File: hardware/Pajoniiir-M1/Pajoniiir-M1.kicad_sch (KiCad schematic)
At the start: 0 parts

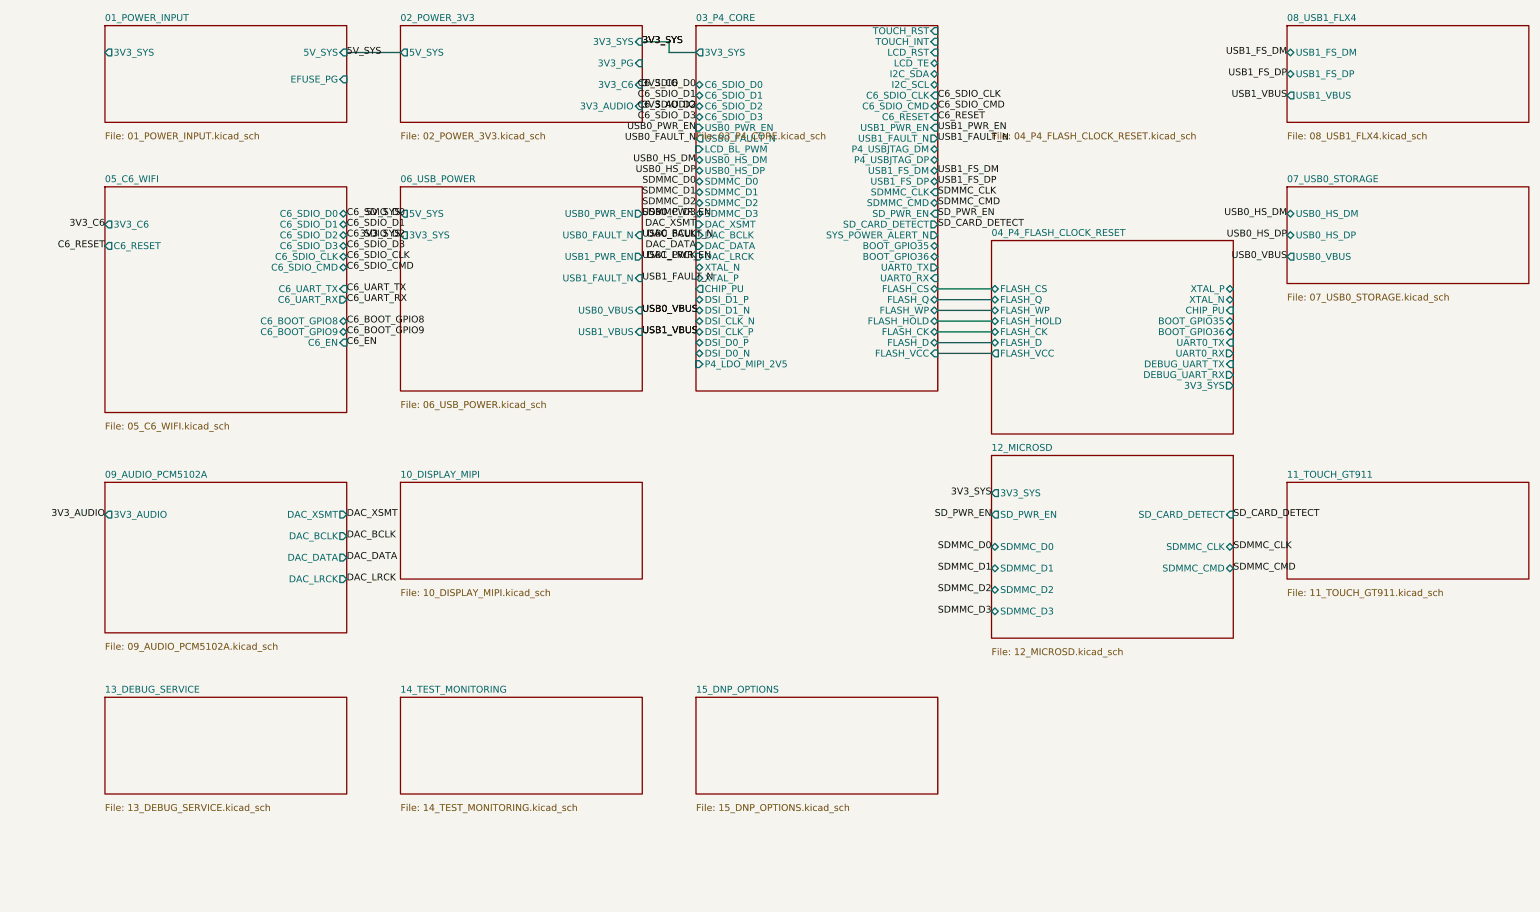
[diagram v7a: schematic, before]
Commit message: hardware: wire debug service hierarchy
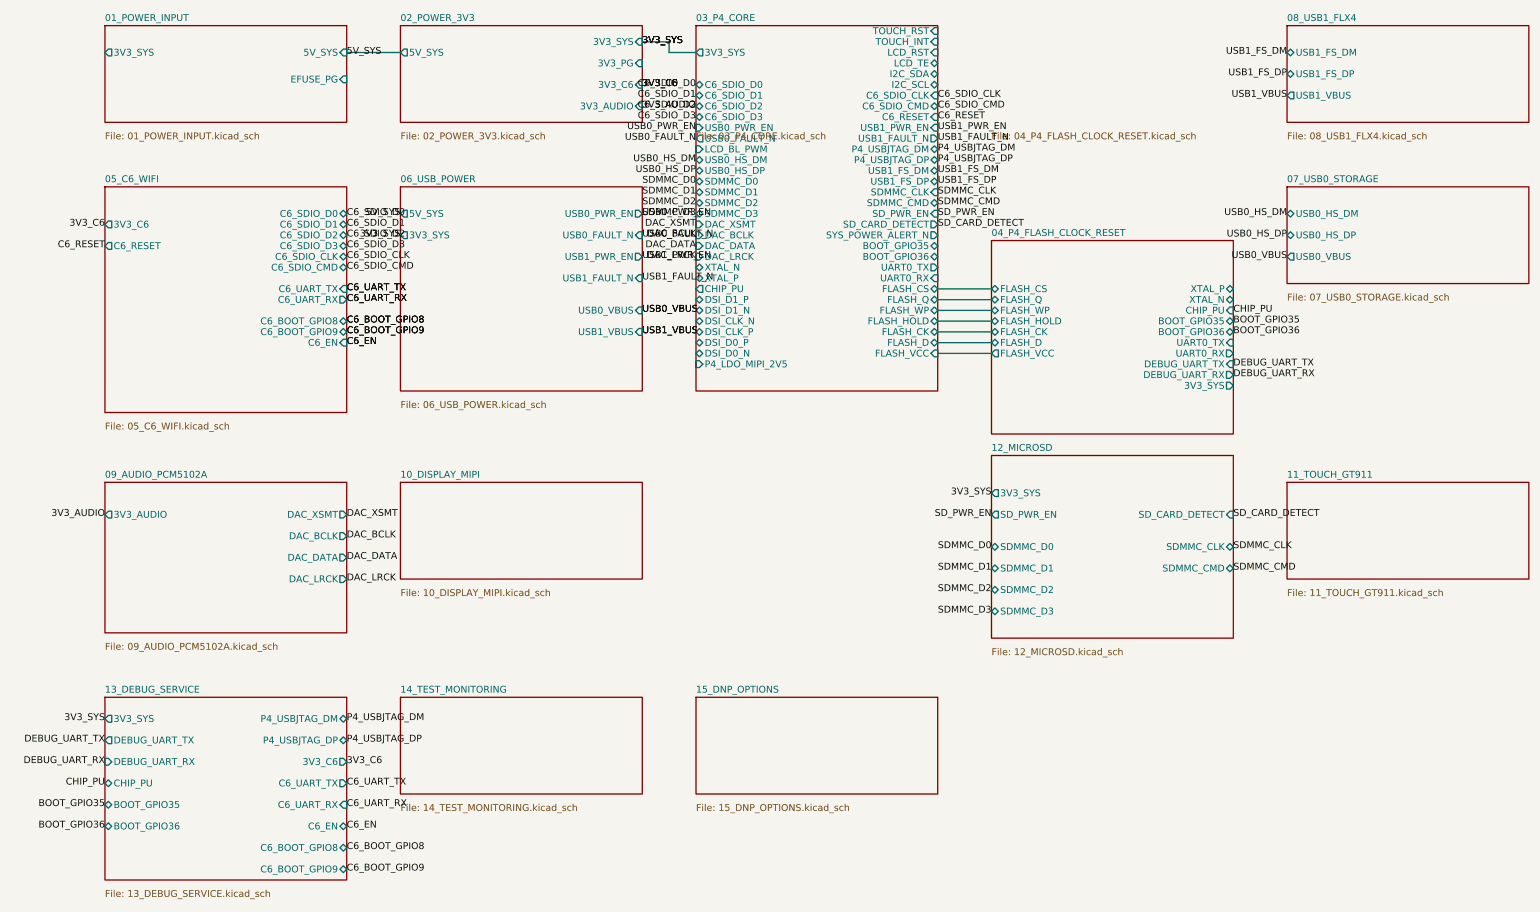
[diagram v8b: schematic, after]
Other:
- sheet 13_DEBUG_SERVICE ports: added 3V3_C6, 3V3_SYS, BOOT_GPIO35, BOOT_GPIO36, C6_BOOT_GPIO8, C6_BOOT_GPIO9, C6_EN, C6_UART_RX, C6_UART_TX, CHIP_PU, DEBUG_UART_RX, DEBUG_UART_TX, P4_USBJTAG_DM, P4_USBJTAG_DP; removed none
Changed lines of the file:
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@@
   (sheet
     (at 20 145)
-    (size 45 18)
+    (size 45 34)
     (fields_autoplaced yes)
     (stroke (width 0.1524) (type solid))
@@
     )
     (property "Sheetfile" "13_DEBUG_SERVICE.kicad_sch"
-      (at 20 164.8246 0)
+      (at 20 180.8246 0)
       (effects (font (size 1.27 1.27)) (justify left top))
     )
+    (pin "3V3_SYS" output (at 20 149 180) (effects (font (size 1.27 1.27)) (justify left)))
+    (pin "DEBUG_UART_TX" output (at 20 153 180) (effects (font (size 1.27 1.27)) (justify left)))
+    (pin "DEBUG_UART_RX" input (at 20 157 180) (effects (font (size 1.27 1.27)) (justify left)))
+    (pin "CHIP_PU" bidirectional (at 20 161 180) (effects (font (size 1.27 1.27)) (justify left)))
+    (pin "BOOT_GPIO35" bidirectional (at 20 165 180) (effects (font (size 1.27 1.27)) (justify left)))
+    (pin "BOOT_GPIO36" bidirectional (at 20 169 180) (effects (font (size 1.27 1.27)) (justify left)))
+    (pin "P4_USBJTAG_DM" bidirectional (at 65 149 0) (effects (font (size 1.27 1.27)) (justify right)))
+    (pin "P4_USBJTAG_DP" bidirectional (at 65 153 0) (effects (font (size 1.27 1.27)) (justify right)))
+    (pin "3V3_C6" output (at 65 157 0) (effects (font (size 1.27 1.27)) (justify right)))
+    (pin "C6_UART_TX" output (at 65 161 0) (effects (font (size 1.27 1.27)) (justify right)))
+    (pin "C6_UART_RX" input (at 65 165 0) (effects (font (size 1.27 1.27)) (justify right)))
+    (pin "C6_EN" bidirectional (at 65 169 0) (effects (font (size 1.27 1.27)) (justify right)))
+    (pin "C6_BOOT_GPIO8" bidirectional (at 65 173 0) (effects (font (size 1.27 1.27)) (justify right)))
+    (pin "C6_BOOT_GPIO9" bidirectional (at 65 177 0) (effects (font (size 1.27 1.27)) (justify right)))
     (instances
       (project "Pajoniiir-M1"
@@
   (label "SDMMC_CLK" (at 175 51 0) (effects (font (size 1.27 1.27))))
   (label "SDMMC_CMD" (at 175 53 0) (effects (font (size 1.27 1.27))))
+  (label "3V3_SYS" (at 20 149 180) (effects (font (size 1.27 1.27))))
+  (label "DEBUG_UART_TX" (at 20 153 180) (effects (font (size 1.27 1.27))))
+  (label "DEBUG_UART_RX" (at 20 157 180) (effects (font (size 1.27 1.27))))
+  (label "CHIP_PU" (at 20 161 180) (effects (font (size 1.27 1.27))))
+  (label "BOOT_GPIO35" (at 20 165 180) (effects (font (size 1.27 1.27))))
+  (label "BOOT_GPIO36" (at 20 169 180) (effects (font (size 1.27 1.27))))
+  (label "P4_USBJTAG_DM" (at 65 149 0) (effects (font (size 1.27 1.27))))
+  (label "P4_USBJTAG_DP" (at 65 153 0) (effects (font (size 1.27 1.27))))
+  (label "3V3_C6" (at 65 157 0) (effects (font (size 1.27 1.27))))
+  (label "C6_UART_TX" (at 65 161 0) (effects (font (size 1.27 1.27))))
+  (label "C6_UART_RX" (at 65 165 0) (effects (font (size 1.27 1.27))))
+  (label "C6_EN" (at 65 169 0) (effects (font (size 1.27 1.27))))
+  (label "C6_BOOT_GPIO8" (at 65 173 0) (effects (font (size 1.27 1.27))))
+  (label "C6_BOOT_GPIO9" (at 65 177 0) (effects (font (size 1.27 1.27))))
+  (label "3V3_SYS" (at 120 23 0) (effects (font (size 1.27 1.27))))
+  (label "DEBUG_UART_TX" (at 230 83 0) (effects (font (size 1.27 1.27))))
+  (label "DEBUG_UART_RX" (at 230 85 0) (effects (font (size 1.27 1.27))))
+  (label "CHIP_PU" (at 230 73 0) (effects (font (size 1.27 1.27))))
+  (label "BOOT_GPIO35" (at 230 75 0) (effects (font (size 1.27 1.27))))
+  (label "BOOT_GPIO36" (at 230 77 0) (effects (font (size 1.27 1.27))))
+  (label "P4_USBJTAG_DM" (at 175 43 0) (effects (font (size 1.27 1.27))))
+  (label "P4_USBJTAG_DP" (at 175 45 0) (effects (font (size 1.27 1.27))))
+  (label "3V3_C6" (at 120 31 0) (effects (font (size 1.27 1.27))))
+  (label "C6_UART_TX" (at 65 69 0) (effects (font (size 1.27 1.27))))
+  (label "C6_UART_RX" (at 65 71 0) (effects (font (size 1.27 1.27))))
+  (label "C6_EN" (at 65 79 0) (effects (font (size 1.27 1.27))))
+  (label "C6_BOOT_GPIO8" (at 65 75 0) (effects (font (size 1.27 1.27))))
+  (label "C6_BOOT_GPIO9" (at 65 77 0) (effects (font (size 1.27 1.27))))
   (sheet_instances (path "/" (page "1")))
   (embedded_fonts no)
